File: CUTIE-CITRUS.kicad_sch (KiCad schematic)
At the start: 1 part, among them J2 F32Q-1A7H1-11022

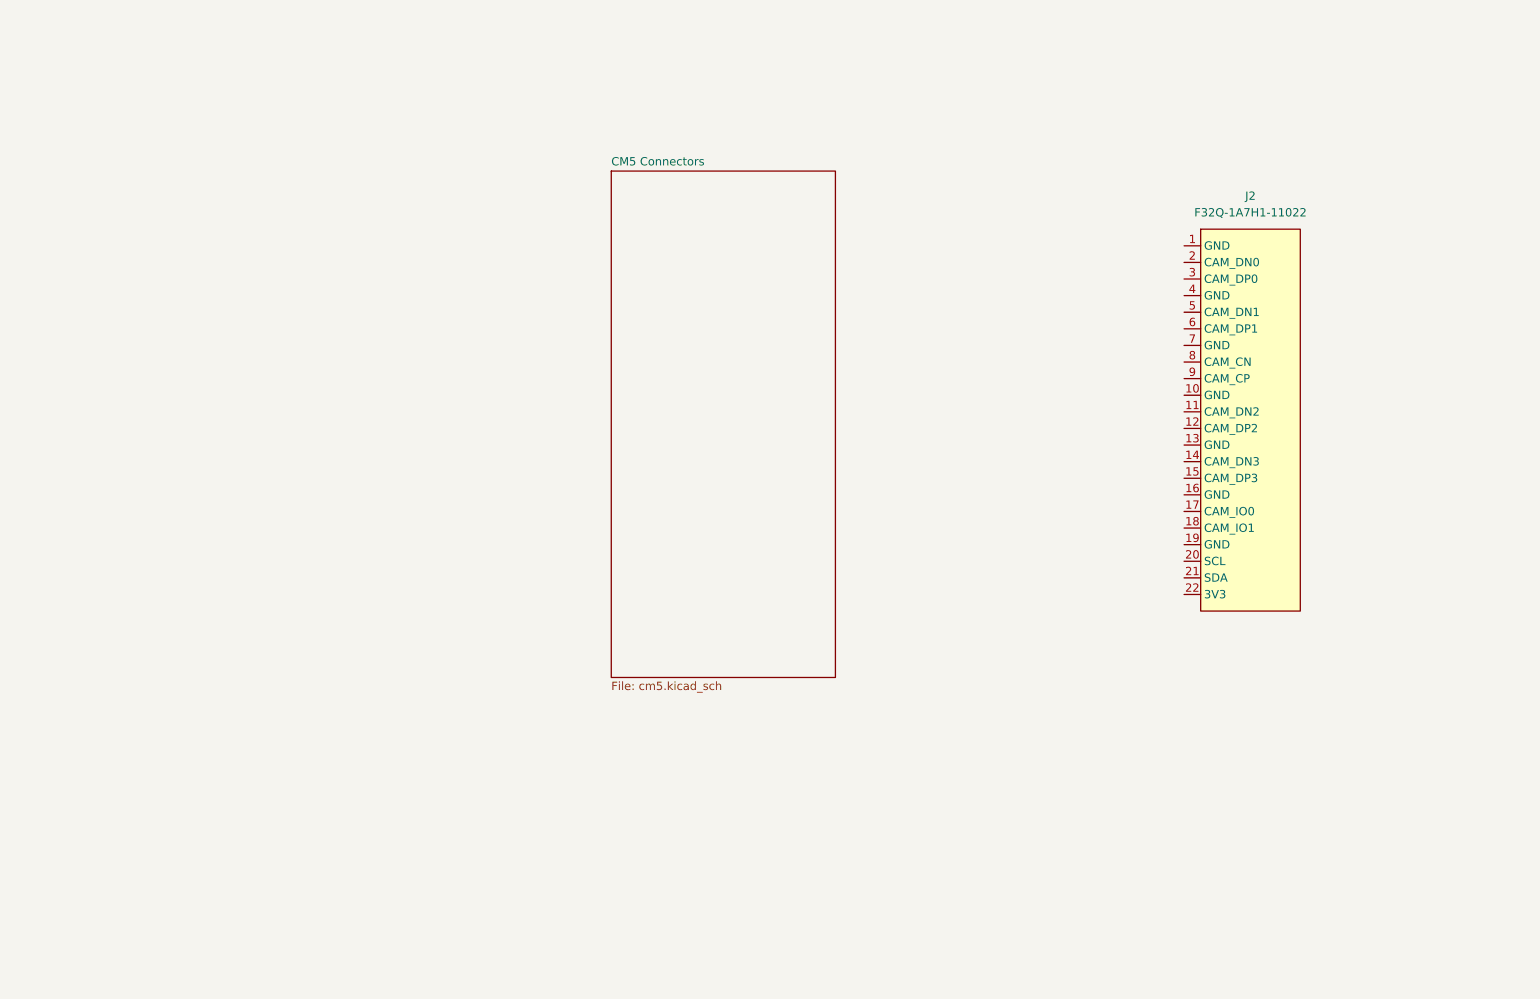
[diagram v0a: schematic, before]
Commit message: added m2 mkey conn, defined signals
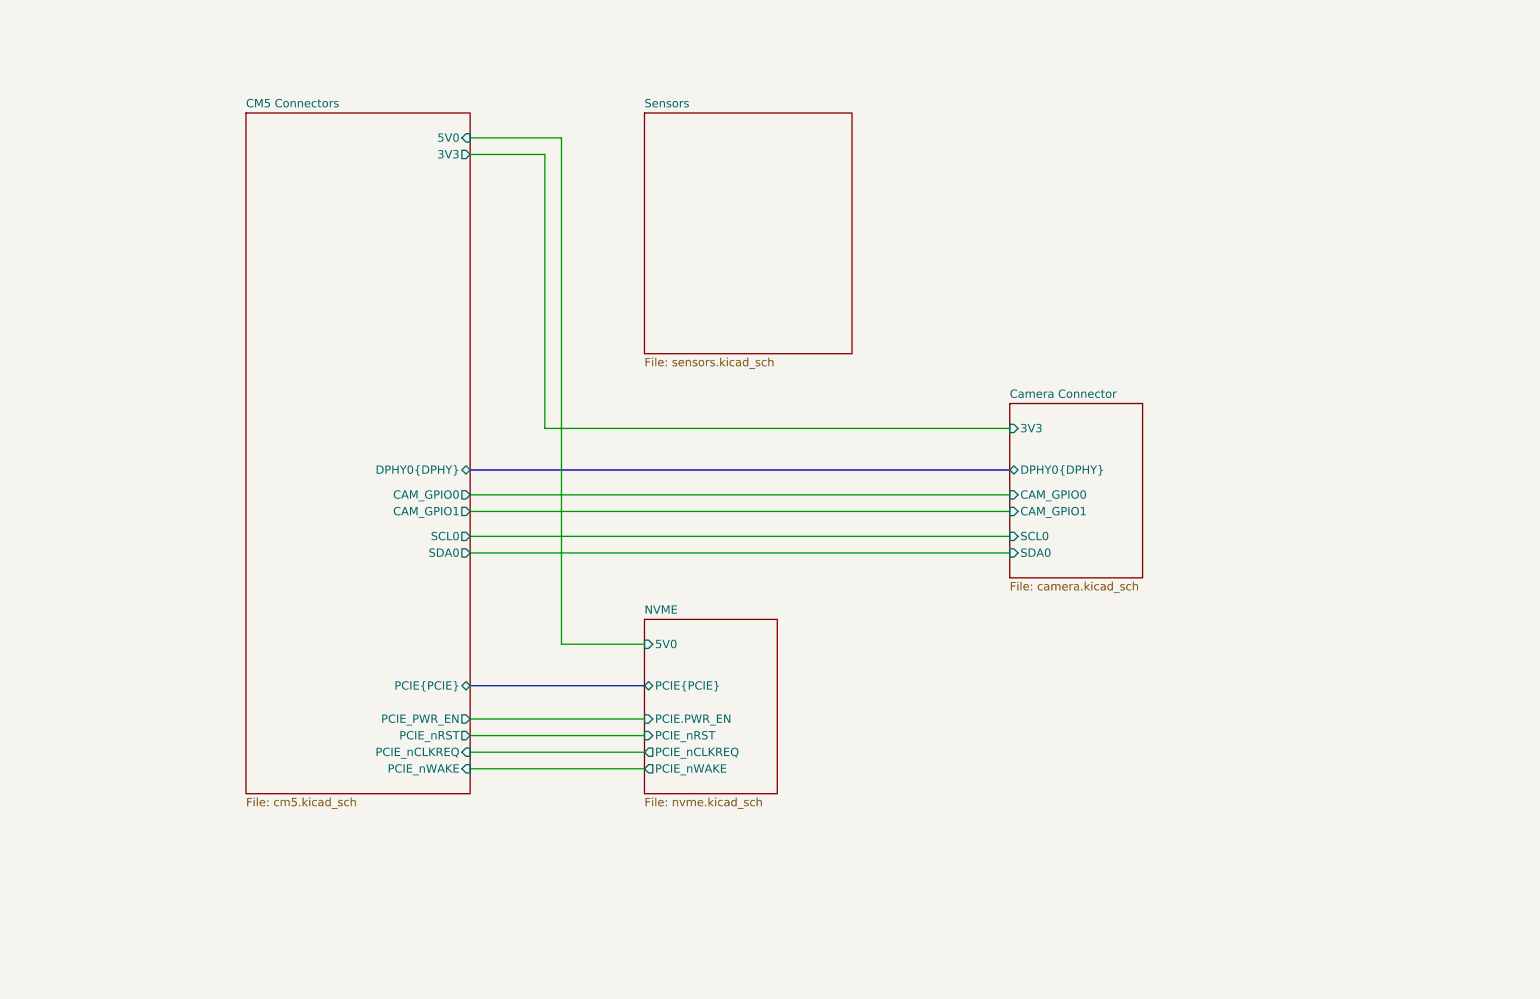
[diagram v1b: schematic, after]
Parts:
- removed J2: F32Q-1A7H1-11022, symbol library:F32Q-1A7H1-11022
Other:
- added sheet Camera Connector (camera.kicad_sch)
- added sheet NVME (nvme.kicad_sch)
- added sheet Sensors (sensors.kicad_sch)
- sheet CM5 Connectors ports: added 3V3, 5V0, CAM_GPIO0, CAM_GPIO1, DPHY0{DPHY}, PCIE_PWR_EN, PCIE_nCLKREQ, PCIE_nRST, PCIE_nWAKE, PCIE{PCIE}, SCL0, SDA0; removed none

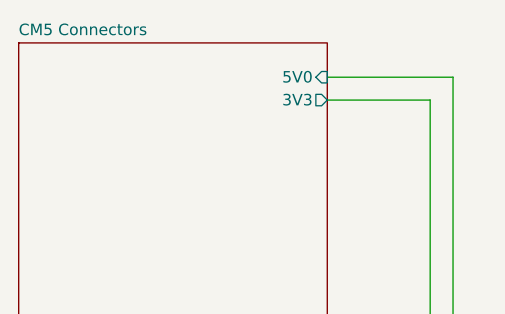
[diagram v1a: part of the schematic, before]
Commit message: restructured symbols, added footprints
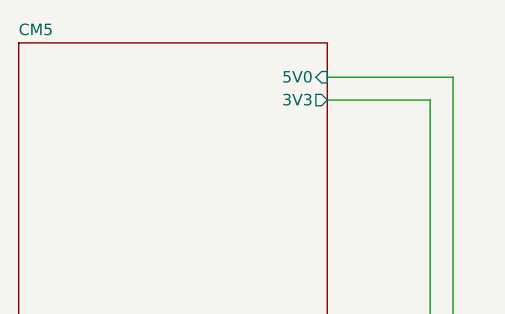
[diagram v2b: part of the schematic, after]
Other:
- sheet CM5 Connectors renamed CM5
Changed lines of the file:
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@@
 			(color 0 0 0 0.0000)
 		)
-		(property "Sheetname" "CM5 Connectors"
+		(property "Sheetname" "CM5"
 			(at 78.74 38.6584 0)
 			(effects

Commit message: quick push, no major change
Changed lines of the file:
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@@
 	(generator_version "9.0")
 	(paper "A4")
+	(junction
+		(at 121.92 43.18)
+		(diameter 0)
+		(color 0 0 0 0)
+	)
+	(junction
+		(at 119.38 45.72)
+		(diameter 0)
+		(color 0 0 0 0)
+	)
 	(wire
 		(pts
@@
 	(wire
 		(pts
-			(xy 113.03 43.18) (xy 127 43.18)
+			(xy 119.38 45.72) (xy 119.38 31.75)
+		)
+		(stroke
+			(width 0.381)
+			(type default)
+			(color 255 153 0 1)
+		)
+	)
+	(wire
+		(pts
+			(xy 113.03 43.18) (xy 121.92 43.18)
 		)
 		(stroke
@@
 	(wire
 		(pts
+			(xy 119.38 45.72) (xy 124.46 45.72)
+		)
+		(stroke
+			(width 0.381)
+			(type default)
+			(color 255 153 0 1)
+		)
+	)
+	(wire
+		(pts
 			(xy 113.03 104.14) (xy 195.58 104.14)
 		)
@@
 		)
 	)
+	(wire
+		(pts
+			(xy 121.92 43.18) (xy 127 43.18)
+		)
+		(stroke
+			(width 0.508)
+			(type default)
+			(color 255 0 0 1)
+		)
+	)
+	(wire
+		(pts
+			(xy 121.92 43.18) (xy 121.92 31.75)
+		)
+		(stroke
+			(width 0.508)
+			(type default)
+			(color 255 0 0 1)
+		)
+	)
 	(bus
 		(pts
@@
 	(wire
 		(pts
-			(xy 113.03 45.72) (xy 124.46 45.72)
+			(xy 113.03 45.72) (xy 119.38 45.72)
 		)
 		(stroke
@@
 	(wire
 		(pts
+			(xy 119.38 31.75) (xy 110.49 31.75)
+		)
+		(stroke
+			(width 0.381)
+			(type default)
+			(color 255 153 0 1)
+		)
+	)
+	(wire
+		(pts
 			(xy 113.03 100.33) (xy 195.58 100.33)
 		)
@@
 		)
 	)
+	(wire
+		(pts
+			(xy 121.92 31.75) (xy 129.54 31.75)
+		)
+		(stroke
+			(width 0.508)
+			(type default)
+			(color 255 0 0 1)
+		)
+	)
+	(symbol
+		(lib_id "power:PWR_FLAG")
+		(at 110.49 31.75 0)
+		(unit 1)
+		(exclude_from_sim no)
+		(in_bom yes)
+		(on_board yes)
+		(dnp no)
+		(fields_autoplaced yes)
+		(property "Reference" "#FLG01"
+			(at 110.49 29.845 0)
+			(effects
+				(font
+					(size 1.27 1.27)
+				)
+				(hide yes)
+			)
+		)
+		(property "Value" "PWR_FLAG"
+			(at 110.49 26.67 0)
+			(effects
+				(font
+					(size 1.27 1.27)
+				)
+			)
+		)
+		(property "Footprint" ""
+			(at 110.49 31.75 0)
+			(effects
+				(font
+					(size 1.27 1.27)
+				)
+				(hide yes)
+			)
+		)
+		(property "Datasheet" "~"
+			(at 110.49 31.75 0)
+			(effects
+				(font
+					(size 1.27 1.27)
+				)
+				(hide yes)
+			)
+		)
+		(property "Description" "Special symbol for telling ERC where power comes from"
+			(at 110.49 31.75 0)
+			(effects
+				(font
+					(size 1.27 1.27)
+				)
+				(hide yes)
+			)
+		)
+		(pin "1"
+		)
+		(instances
+			(project ""
+				(path "/40af415e-5e3a-41a5-ab07-08c2181863e4"
+					(reference "#FLG01")
+					(unit 1)
+				)
+			)
+		)
+	)
+	(symbol
+		(lib_id "power:PWR_FLAG")
+		(at 129.54 31.75 0)
+		(unit 1)
+		(exclude_from_sim no)
+		(in_bom yes)
+		(on_board yes)
+		(dnp no)
+		(fields_autoplaced yes)
+		(property "Reference" "#FLG02"
+			(at 129.54 29.845 0)
+			(effects
+				(font
+					(size 1.27 1.27)
+				)
+				(hide yes)
+			)
+		)
+		(property "Value" "PWR_FLAG"
+			(at 129.54 26.67 0)
+			(effects
+				(font
+					(size 1.27 1.27)
+				)
+			)
+		)
+		(property "Footprint" ""
+			(at 129.54 31.75 0)
+			(effects
+				(font
+					(size 1.27 1.27)
+				)
+				(hide yes)
+			)
+		)
+		(property "Datasheet" "~"
+			(at 129.54 31.75 0)
+			(effects
+				(font
+					(size 1.27 1.27)
+				)
+				(hide yes)
+			)
+		)
+		(property "Description" "Special symbol for telling ERC where power comes from"
+			(at 129.54 31.75 0)
+			(effects
+				(font
+					(size 1.27 1.27)
+				)
+				(hide yes)
+			)
+		)
+		(pin "1"
+		)
+		(instances
+			(project "CUTIE-CITRUS"
+				(path "/40af415e-5e3a-41a5-ab07-08c2181863e4"
+					(reference "#FLG02")
+					(unit 1)
+				)
+			)
+		)
+	)

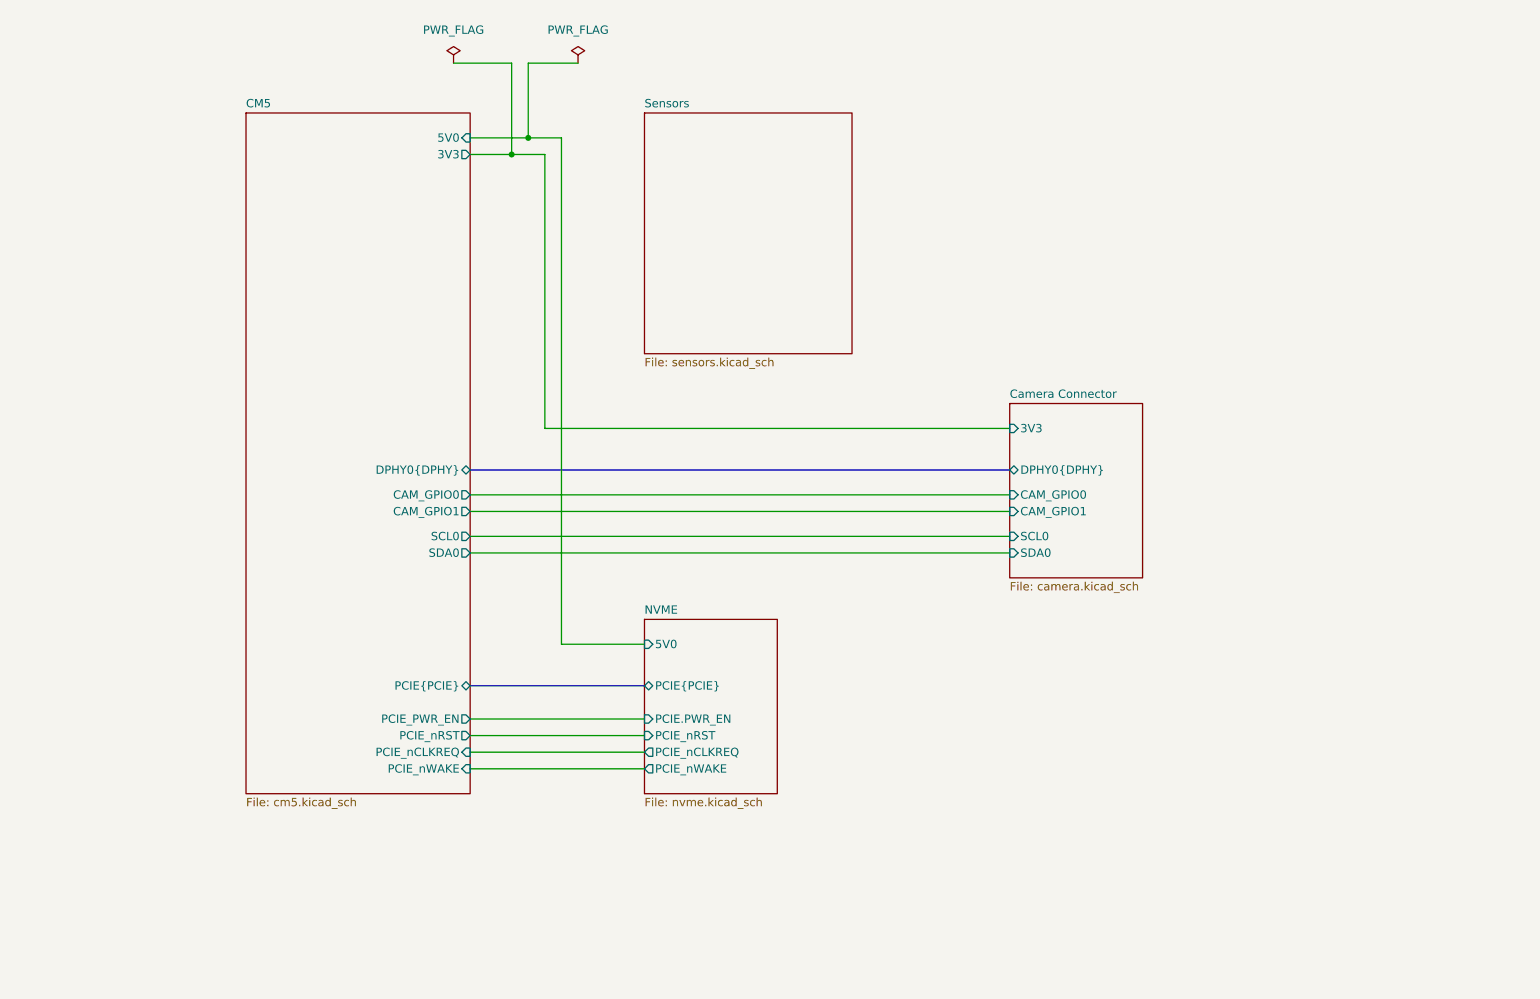
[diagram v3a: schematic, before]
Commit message: added second camera, 6-axis imu
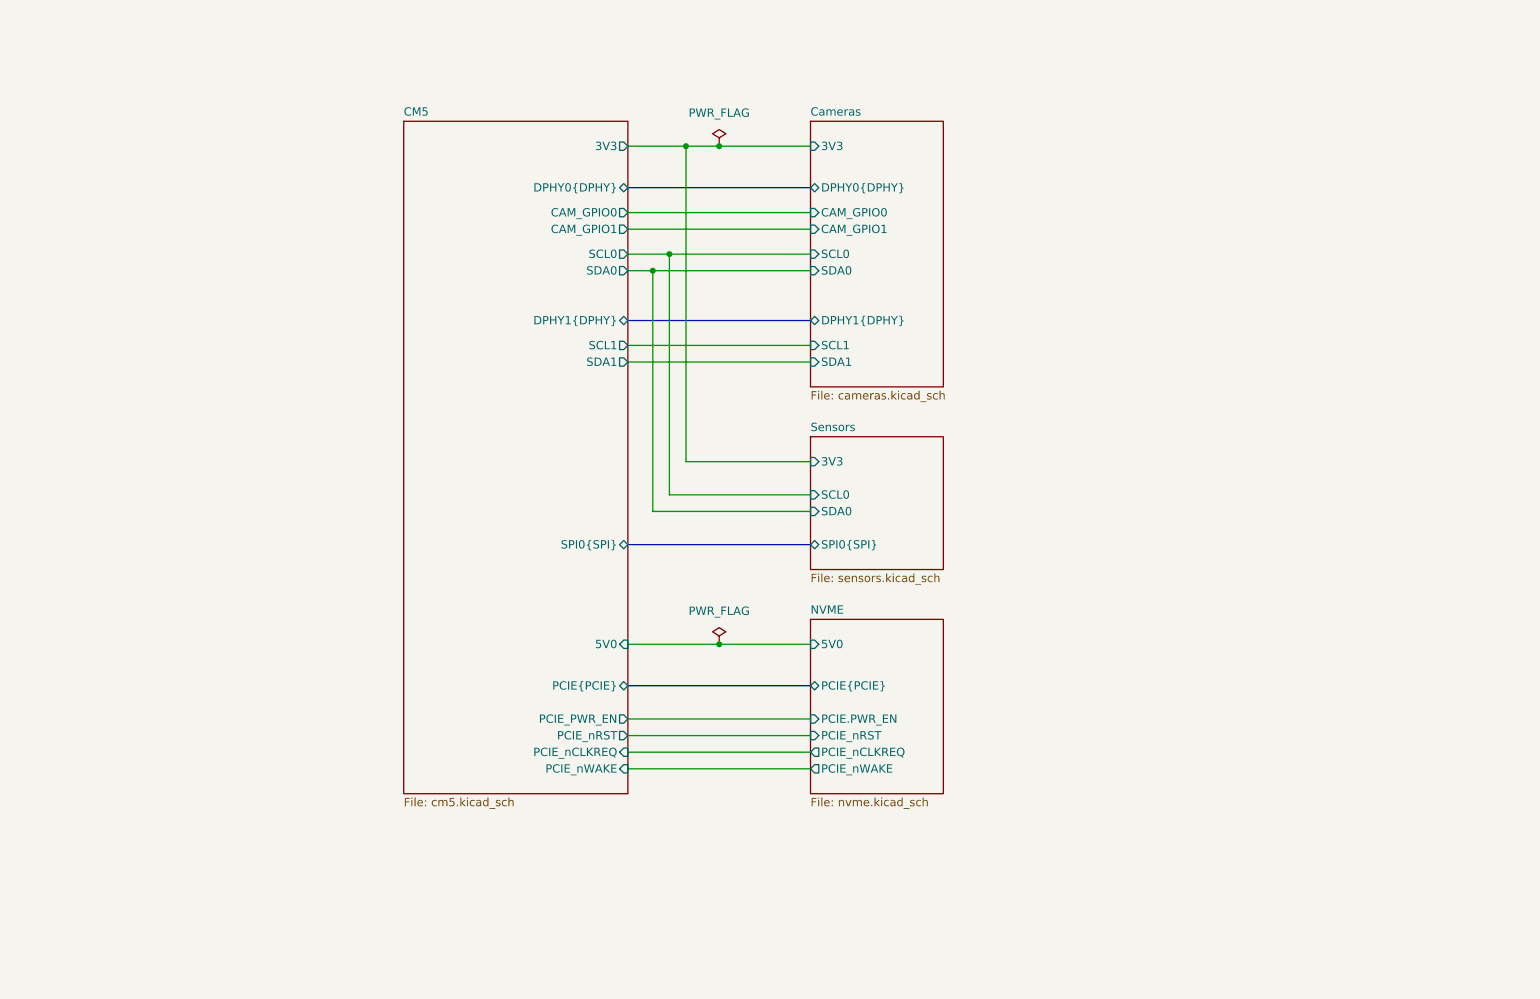
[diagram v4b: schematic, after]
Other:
- sheet Camera Connector renamed Cameras
- sheet CM5 ports: added DPHY1{DPHY}, SCL1, SDA1, SPI0{SPI}; removed none
- sheet Cameras: file camera.kicad_sch -> cameras.kicad_sch
- sheet Cameras ports: added DPHY1{DPHY}, SCL1, SDA1; removed none
- sheet Sensors ports: added 3V3, SCL0, SDA0, SPI0{SPI}; removed none

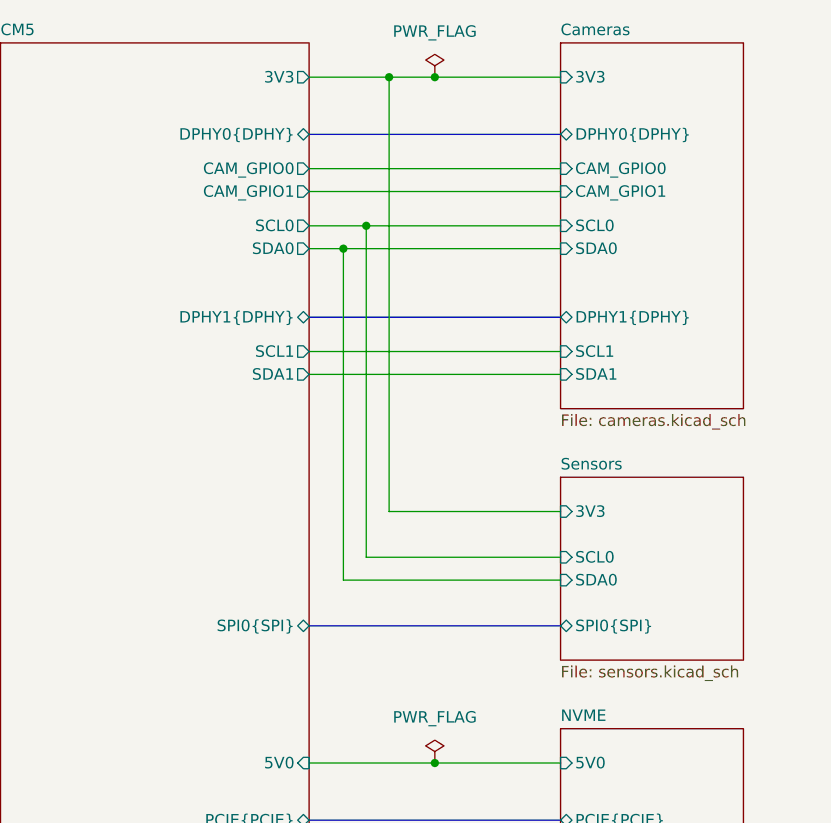
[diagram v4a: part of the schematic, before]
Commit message: extra abstraction layer for cm5 conns.
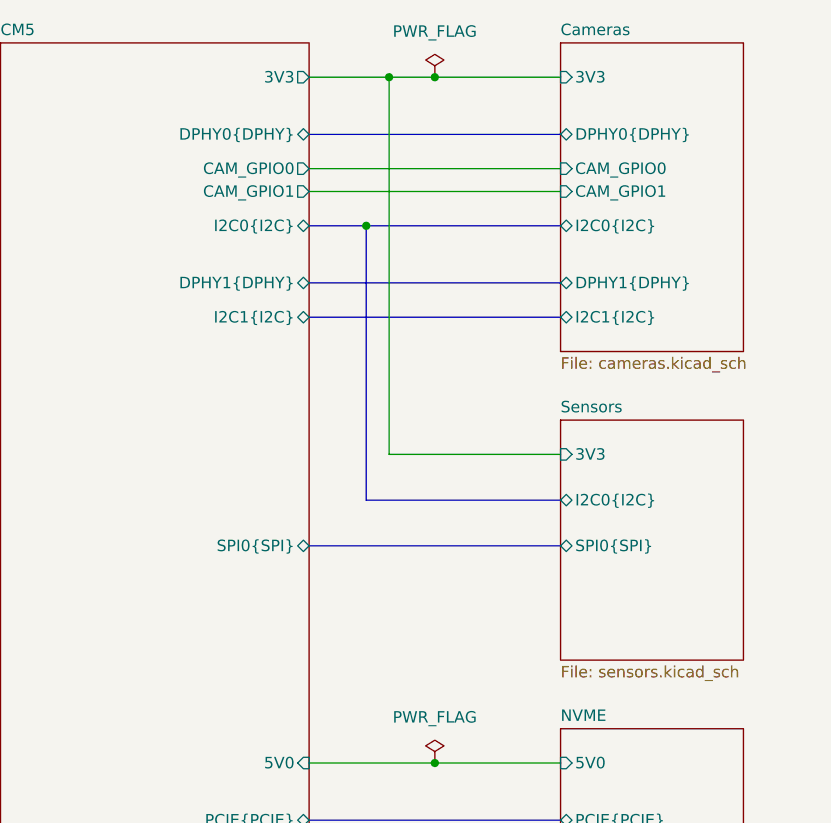
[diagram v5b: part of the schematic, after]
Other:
- sheet CM5 ports: added I2C0{I2C}, I2C1{I2C}; removed SCL0, SCL1, SDA0, SDA1
- sheet Cameras ports: added I2C0{I2C}, I2C1{I2C}; removed SCL0, SCL1, SDA0, SDA1
- sheet Sensors ports: added I2C0{I2C}; removed SCL0, SDA0
- company: (none) -> Andre S Winkel | Highlander Space Program | University of California, Riverside
- title: (none) -> CUTIE-CITRUS PCB
